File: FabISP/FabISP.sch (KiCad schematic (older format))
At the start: 10 parts

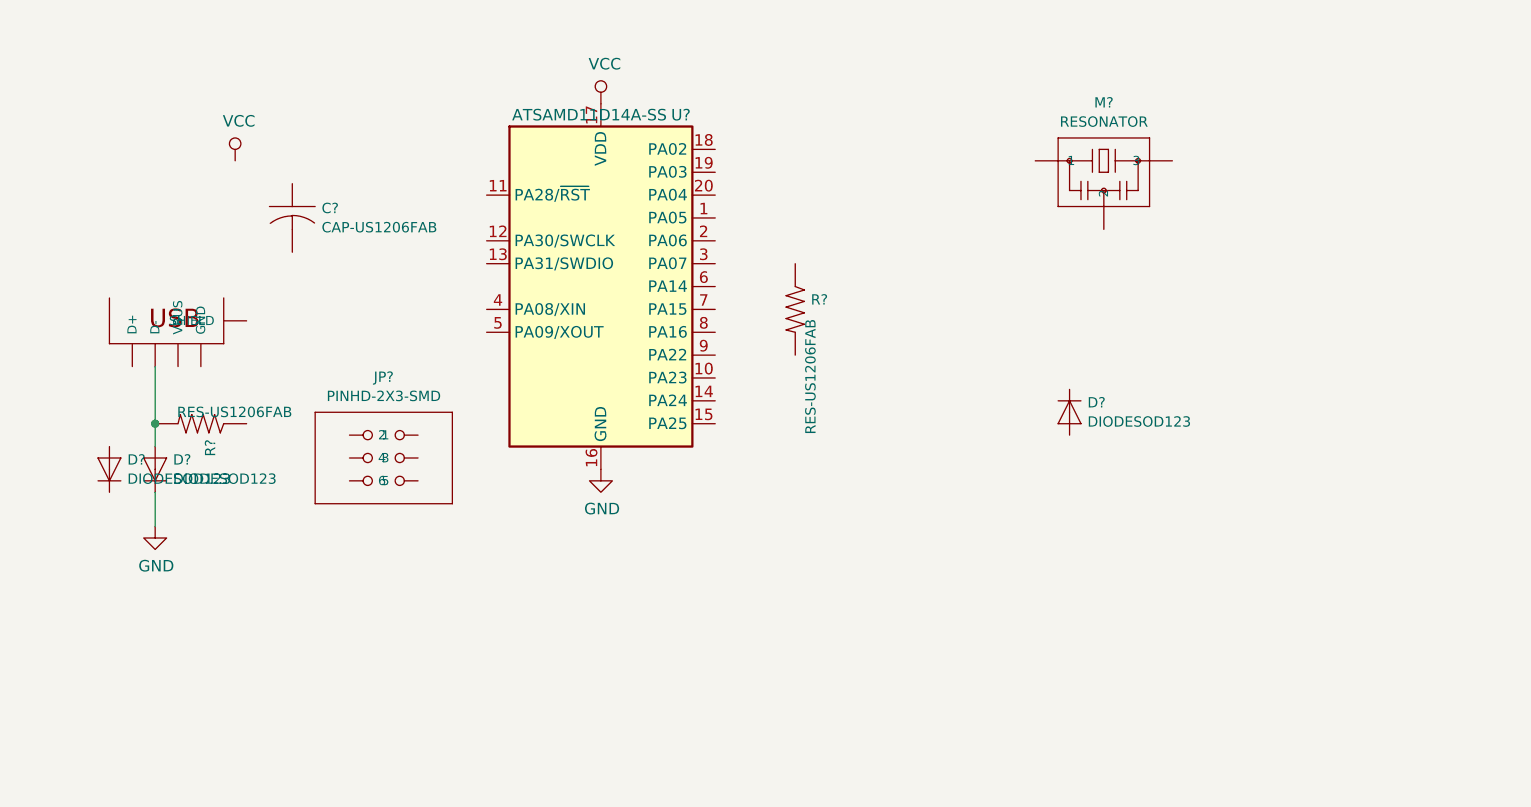
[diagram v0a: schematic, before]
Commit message: avance de conexiones
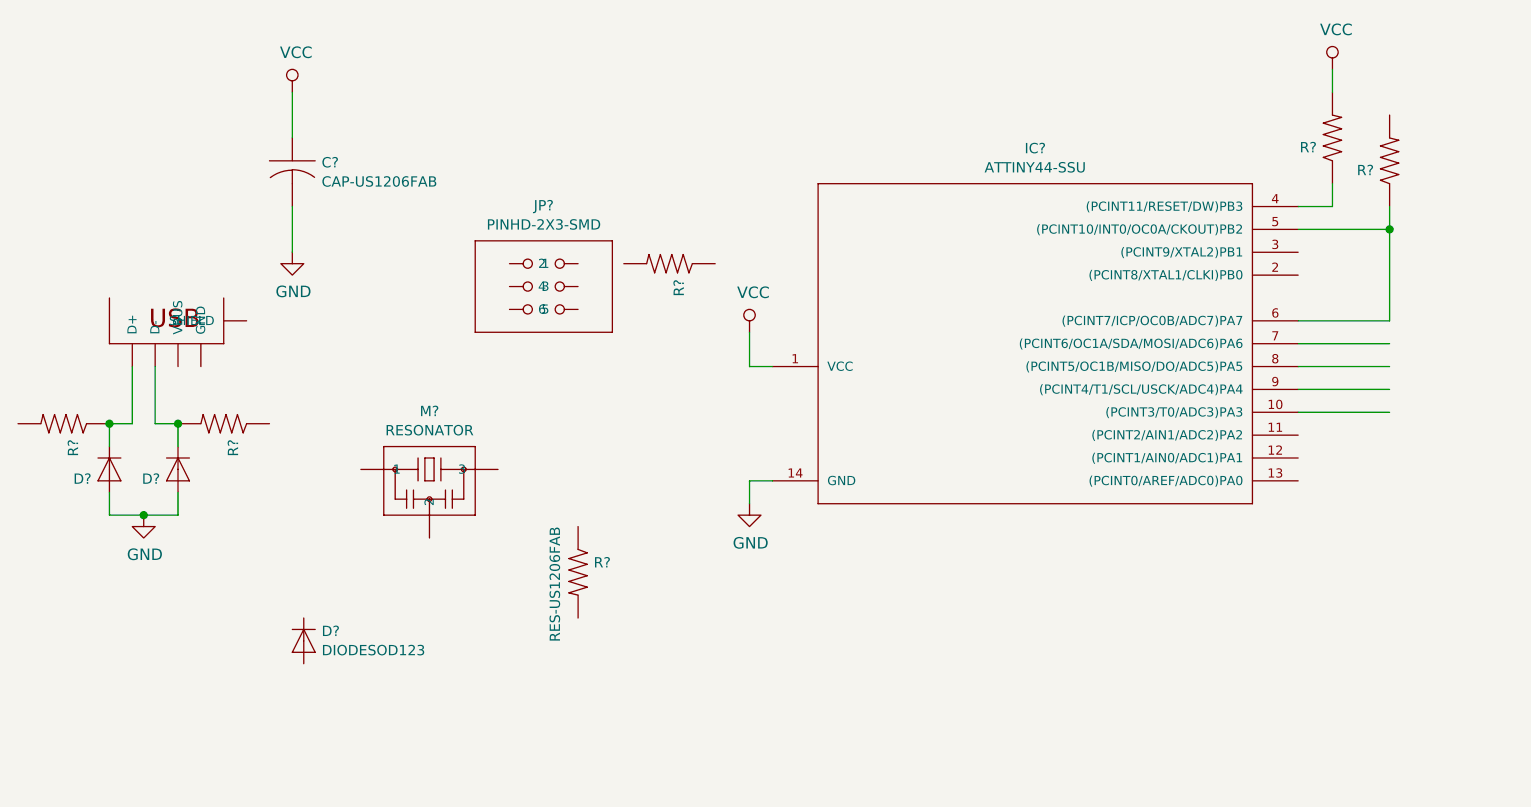
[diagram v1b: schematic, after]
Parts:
- removed U?: ATSAMD11D14A-SS, fab:fab-SOIC-20_7.5x12.8mm_P1.27mm, symbol fab:ATSAMD11D14A-SS
- added IC?: ATTINY44-SSU, fab:fab-SOIC-14_3.9x8.7mm_P1.27mm, symbol fab:ATTINY44-SSU
- added R? (x4): RES-US1206FAB, fab:fab-R1206FAB, symbol fab:RES-US1206FAB
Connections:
- wire segments 3 -> 27
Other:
- moved on the sheet: C?, D?, JP?, M?, R?

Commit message: .
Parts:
- added M2: LEDFAB1206, fab:fab-LED1206FAB, symbol fab:LEDFAB1206
- added R1: RES-US1206FAB, fab:fab-R1206FAB, symbol fab:RES-US1206FAB
- gave numbers to parts that had none: 14
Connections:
- wire segments 27 -> 34
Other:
- moved on the sheet: C1, D1, D2, D3, IC1, JP1, M3, R2, R3, R4, R5, R6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
